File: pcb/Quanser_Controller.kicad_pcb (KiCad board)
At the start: 2 copper layers, 115.6 x 61 mm, 19 parts, among them J1 Conn_02x08, J2 Connector Encoder, J3 Conn_01x10, J4 Conn_01x08, J5 Conn_01x08, J6 Conn_Coaxial, J7 Screw_Terminal_01x02, U1 LMD18200, U2 LS7366R, U3 74LVC1G04

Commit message: Update project.
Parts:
- added F1: 5A, Fuse:Fuseholder_Cylinder-5x20mm_Schurter_0031_8201_Horizontal_Open, F.Cu at (203.6, 102.3)
- added J6: Screw_Terminal_01x02, TerminalBlock:TerminalBlock_Altech_AK300-2_P5.00mm, F.Cu at (157.7, 145.6)
- added Q1: BC548, Package_TO_SOT_THT:TO-92_Inline, F.Cu at (114.0, 140.6)
- added R4: 5K, Resistor_THT:R_Axial_DIN0204_L3.6mm_D1.6mm_P5.08mm_Horizontal, F.Cu at (176.0, 142.5)
- added R5: 2K, Resistor_THT:R_Axial_DIN0204_L3.6mm_D1.6mm_P5.08mm_Horizontal, F.Cu at (176.0, 145.6)
- F1: value Fuse -> 5A
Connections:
- J1 pad 1: Net-(J1-Pad1) -> GND
- J1 pad 11: Net-(J1-Pad11) -> GND
- J1 pad 13: Net-(J1-Pad13) -> GND
- J1 pad 15: Net-(J1-Pad15) -> GND
- J1 pad 3: Net-(J1-Pad3) -> GND
- J1 pad 5: Net-(J1-Pad5) -> GND
- J1 pad 7: Net-(J1-Pad7) -> GND
- J1 pad 9: Net-(J1-Pad9) -> GND
- J4 pad 4: ENABLE -> DISABLE
- J4 pad 8: Net-(J4-Pad8) -> BRAKE
- U1 pad 4: Net-(U1-Pad4) -> BRAKE
- U1 pad 6: Net-(F1-Pad2) -> Net-(F1-Pad1)

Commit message: update pcb
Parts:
- removed the F1 at (203.6, 102.3)
- removed the F1 at (125.8, 129.7)
- removed the J6 at (157.7, 145.6)
- removed the J6 at (83.1, 107.7)
- removed U3: 74LVC1G04, Connector_PinHeader_2.00mm:PinHeader_2x03_P2.00mm_Vertical
- added F1: 5A, Fuse:Fuseholder_Cylinder-5x20mm_Schurter_0031_8201_Horizontal_Open, F.Cu at (154.9, 76.2)
- added J6: Screw_Terminal_01x02, TerminalBlock:TerminalBlock_Altech_AK300-2_P5.00mm, F.Cu at (97.8, 61.0)
- J7: footprint Connector_PinHeader_2.00mm:PinHeader_1x02_P2.00mm_Vertical -> TerminalBlock:TerminalBlock_Altech_AK300-2_P5.00mm
- moved R5 98.3 mm to (135.9, 55.9)
- moved J7 84.3 mm to (120.7, 61.0)
- moved J2 79.6 mm to (198.1, 59.7)
- moved R4 69.2 mm to (132.1, 88.9), turned to 270 degrees
- moved R2 66.0 mm to (118.1, 88.9), turned to 0 degrees
- moved Q1 64.2 mm to (138.4, 81.3), turned to 90 degrees
- moved J5 58.7 mm to (182.9, 53.3), turned to 90 degrees
- moved J1 56.1 mm to (97.8, 97.8)
- moved J4 53.7 mm to (97.8, 88.9), turned to 90 degrees
- moved C3 52.8 mm to (97.8, 73.7)
- moved C4 49.7 mm to (142.2, 68.6), turned to 90 degrees
- moved U1 46.0 mm to (108.0, 80.0)
- moved U2 43.1 mm to (176.5, 73.7), turned to 90 degrees
- moved R3 39.0 mm to (97.8, 85.1), turned to 90 degrees
- moved C2 34.8 mm to (170.2, 88.9)
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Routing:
- net GND: track 139.3 -> 0.62 mm
- net Net-(R2-Pad2): track 69.0 -> 15.4 mm
- net Net-(F1-Pad1): track 0.00 -> 42.2 mm
- net DISABLE: track 0.00 -> 30.4 mm
- net +5V: track 104.6 -> 125.0 mm
- net Net-(C1-Pad1): track 29.7 -> 47.6 mm
- net Net-(F1-Pad2): track 25.8 -> 43.0 mm
- net TH_FLAG: track 44.2 -> 29.0 mm
- net Net-(U1-Pad4): track 14.7 -> 0.00 mm
- net BRAKE: track 0.00 -> 14.5 mm
- net Net-(C4-Pad2): track 34.6 -> 48.9 mm
- net PWM: track 22.4 -> 9.54 mm
- net Net-(Q1-Pad2): track 0.00 -> 12.2 mm
- net #SS: track 12.0 -> 24.1 mm
- net ENABLE: track 9.76 -> 0.00 mm
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- added copper zone on B.Cu, net GND
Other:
- board size 115.6 x 61 mm -> 114.3 x 50.8 mm

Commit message: update PCB; included reports; add A/D
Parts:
- added AD1: Conn_01x06, Connector_PinHeader_2.00mm:PinHeader_1x06_P2.00mm_Vertical, F.Cu at (92.7, 80.0)
- added R6: 1K, Resistor_THT:R_Axial_DIN0204_L3.6mm_D1.6mm_P5.08mm_Horizontal, F.Cu at (149.9, 86.4)
- added R7: 1K, Resistor_THT:R_Axial_DIN0204_L3.6mm_D1.6mm_P5.08mm_Horizontal, F.Cu at (135.9, 99.1)
- R4: value 5K -> 4K3
- R5: value 2K -> 5K
- moved R5 41.9 mm to (125.7, 96.5), turned to 180 degrees
- moved F1 22.9 mm to (154.9, 53.3), turned to 270 degrees
- turned C1 to 270 degrees
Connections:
- net Net-(R2-Pad2) renamed AD
- F1 pad 1: Net-(F1-Pad1) -> +28V
- J4 pad 4: DISABLE -> ENABLE
- J4 pad 8: BRAKE -> Net-(J4-Pad8)
- Q1 pad 1: Net-(F1-Pad2) -> Net-(Q1-Pad1)
- R4 pad 2: DISABLE -> ENABLE
- R5 pad 1: +28V -> Net-(Q1-Pad2)
- R5 pad 2: Net-(F1-Pad2) -> GND
- U1 pad 4: BRAKE -> Net-(Q1-Pad1)
- U1 pad 5: +5V -> ENABLE
- U1 pad 6: Net-(F1-Pad1) -> Net-(F1-Pad2)
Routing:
- net ENABLE: track 0.00 -> 96.9 mm
- net Net-(Q1-Pad1): track 0.00 -> 88.7 mm
- net Net-(F1-Pad1): track 42.2 -> 0.00 mm
- net DISABLE: track 30.4 -> 0.00 mm
- net AD: track 15.4 -> 44.5 mm
- net +28V: track 17.3 -> 44.9 mm
- net BRAKE: track 14.5 -> 0.00 mm
- net Net-(Q1-Pad2): track 12.2 -> 23.9 mm
- net GND: track 0.62 -> 9.29 mm
- net +5V: track 125.0 -> 129.8 mm
- net TH_FLAG: track 29.0 -> 31.5 mm
- net Net-(J2-Pad4): track 12.7 -> 11.2 mm
- net Net-(J2-Pad5): track 12.7 -> 11.2 mm
- net Net-(C2-Pad1): track 39.1 -> 40.1 mm
- net Net-(J4-Pad8): track 0.00 -> 1.00 mm
- removed copper zone on B.Cu, net GND
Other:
- net class Default: clearance 0.2 -> 0.1778; trace_width 0.25 -> 0.2
- rule trace_clearance: 0.2 -> 0.1778

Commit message: Last update PCB
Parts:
- removed AD1: Conn_01x06, Connector_PinHeader_2.00mm:PinHeader_1x06_P2.00mm_Vertical
- added J8: Conn_01x06, Connector_PinHeader_2.00mm:PinHeader_1x06_P2.00mm_Vertical, F.Cu at (92.7, 81.3)
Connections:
- J4 pad 3: TH_FLAG -> PWM
- J4 pad 7: PWM -> TH_FLAG
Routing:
- net PWM: track 9.54 -> 13.4 mm
- net TH_FLAG: track 31.5 -> 30.9 mm
- net AD: track 44.5 -> 44.0 mm
- added copper zone on F.Cu, net GND
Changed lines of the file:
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@@
     (thickness 1.6)
     (drawings 4)
-    (tracks 140)
+    (tracks 144)
     (zones 0)
     (modules 24)
@@
   (net 47 "Net-(Q1-Pad1)")
   (net 48 AD)
-  (net 49 "Net-(AD1-Pad2)")
-  (net 50 "Net-(AD1-Pad3)")
-  (net 51 "Net-(AD1-Pad4)")
-  (net 52 "Net-(AD1-Pad5)")
-  (net 53 "Net-(AD1-Pad1)")
+  (net 49 "Net-(J8-Pad1)")
+  (net 50 "Net-(J8-Pad2)")
+  (net 51 "Net-(J8-Pad3)")
+  (net 52 "Net-(J8-Pad4)")
+  (net 53 "Net-(J8-Pad5)")
   (net_class Default "This is the default net class."
     (clearance 0.1778)
@@
     (add_net MISO)
     (add_net MOSI)
-    (add_net "Net-(AD1-Pad1)")
-    (add_net "Net-(AD1-Pad2)")
-    (add_net "Net-(AD1-Pad3)")
-    (add_net "Net-(AD1-Pad4)")
-    (add_net "Net-(AD1-Pad5)")
     (add_net "Net-(C1-Pad1)")
     (add_net "Net-(C2-Pad1)")
@@
     (add_net "Net-(J5-Pad4)")
     (add_net "Net-(J5-Pad8)")
+    (add_net "Net-(J8-Pad1)")
+    (add_net "Net-(J8-Pad2)")
+    (add_net "Net-(J8-Pad3)")
+    (add_net "Net-(J8-Pad4)")
+    (add_net "Net-(J8-Pad5)")
     (add_net "Net-(Q1-Pad1)")
     (add_net "Net-(Q1-Pad2)")
@@
       (net 32 "Net-(J4-Pad2)"))
     (pad 3 thru_hole oval (at 0 4 90) (size 1.35 1.35) (drill 0.8) (layers *.Cu *.Mask)
-      (net 33 TH_FLAG))
+      (net 34 PWM))
     (pad 4 thru_hole oval (at 0 6 90) (size 1.35 1.35) (drill 0.8) (layers *.Cu *.Mask)
       (net 45 ENABLE))
@@
       (net 12 ELB2))
     (pad 7 thru_hole oval (at 0 12 90) (size 1.35 1.35) (drill 0.8) (layers *.Cu *.Mask)
-      (net 34 PWM))
+      (net 33 TH_FLAG))
     (pad 8 thru_hole oval (at 0 14 90) (size 1.35 1.35) (drill 0.8) (layers *.Cu *.Mask)
       (net 46 "Net-(J4-Pad8)"))
@@
   )
   (module Connector_PinHeader_2.00mm:PinHeader_1x06_P2.00mm_Vertical (layer F.Cu)
-    (at 92.71 80.01 180)
+    (at 92.71 81.28 180)
     (descr "Through hole straight pin header, 1x06, 2.00mm pitch, single row")
     (tags "Through hole pin header THT 1x06 2.00mm single row")
-    (fp_text reference AD1 (at 0 -2.06 180) (layer F.SilkS)
+    (fp_text reference J8 (at 0 -2.06 180) (layer F.SilkS)
       (effects (font (size 1 1) (thickness 0.15)))
     )
@@
     )
     (pad 1 thru_hole rect (at 0 0 180) (size 1.35 1.35) (drill 0.8) (layers *.Cu *.Mask)
-      (net 53 "Net-(AD1-Pad1)"))
+      (net 49 "Net-(J8-Pad1)"))
     (pad 2 thru_hole oval (at 0 2 180) (size 1.35 1.35) (drill 0.8) (layers *.Cu *.Mask)
-      (net 49 "Net-(AD1-Pad2)"))
+      (net 50 "Net-(J8-Pad2)"))
     (pad 3 thru_hole oval (at 0 4 180) (size 1.35 1.35) (drill 0.8) (layers *.Cu *.Mask)
-      (net 50 "Net-(AD1-Pad3)"))
+      (net 51 "Net-(J8-Pad3)"))
     (pad 4 thru_hole oval (at 0 6 180) (size 1.35 1.35) (drill 0.8) (layers *.Cu *.Mask)
-      (net 51 "Net-(AD1-Pad4)"))
+      (net 52 "Net-(J8-Pad4)"))
     (pad 5 thru_hole oval (at 0 8 180) (size 1.35 1.35) (drill 0.8) (layers *.Cu *.Mask)
-      (net 52 "Net-(AD1-Pad5)"))
+      (net 53 "Net-(J8-Pad5)"))
     (pad 6 thru_hole oval (at 0 10 180) (size 1.35 1.35) (drill 0.8) (layers *.Cu *.Mask)
       (net 48 AD))
@@
   (segment (start 184.15 73.66) (end 184.15 72.39) (width 0.25) (layer B.Cu) (net 28))
   (segment (start 184.15 72.39) (end 186.69 69.85) (width 0.25) (layer B.Cu) (net 28))
-  (segment (start 97.79 85.09) (end 101.6 88.9) (width 0.25) (layer F.Cu) (net 33))
-  (segment (start 101.6 88.9) (end 101.79 88.9) (width 0.25) (layer F.Cu) (net 33))
-  (segment (start 121.55 80.01) (end 121.55 84.19) (width 0.25) (layer F.Cu) (net 33))
-  (segment (start 121.55 84.19) (end 119.38 86.36) (width 0.25) (layer F.Cu) (net 33))
-  (segment (start 104.33 86.36) (end 101.79 88.9) (width 0.25) (layer F.Cu) (net 33))
-  (segment (start 119.38 86.36) (end 104.33 86.36) (width 0.25) (layer F.Cu) (net 33))
-  (segment (start 132.08 93.98) (end 108.87 93.98) (width 0.25) (layer F.Cu) (net 45))
-  (segment (start 108.87 93.98) (end 103.79 88.9) (width 0.25) (layer F.Cu) (net 45))
-  (segment (start 111.35 80.01) (end 111.35 81.2353) (width 0.25) (layer B.Cu) (net 34))
-  (segment (start 111.35 81.2353) (end 109.79 82.7953) (width 0.25) (layer B.Cu) (net 34))
-  (segment (start 109.79 82.7953) (end 109.79 88.9) (width 0.25) (layer B.Cu) (net 34))
-  (segment (start 111.79 88.9) (end 111.79 87.8997) (width 0.25) (layer B.Cu) (net 46))
+  (segment (start 109.79 87.945406) (end 112.645406 85.09) (width 0.2) (layer F.Cu) (net 33))
+  (segment (start 120.650001 80.909999) (end 121.55 80.01) (width 0.2) (layer F.Cu) (net 33))
+  (segment (start 119.38 85.09) (end 120.65 83.82) (width 0.2) (layer F.Cu) (net 33))
+  (segment (start 109.79 88.9) (end 109.79 87.945406) (width 0.2) (layer F.Cu) (net 33))
+  (segment (start 120.65 83.82) (end 120.650001 80.909999) (width 0.2) (layer F.Cu) (net 33))
+  (segment (start 112.645406 85.09) (end 119.38 85.09) (width 0.2) (layer F.Cu) (net 33))
+  (segment (start 109.79 87.945406) (end 109.535406 87.945406) (width 0.2) (layer F.Cu) (net 33))
+  (segment (start 106.68 85.09) (end 97.79 85.09) (width 0.2) (layer F.Cu) (net 33))
+  (segment (start 109.535406 87.945406) (end 106.68 85.09) (width 0.2) (layer F.Cu) (net 33))
+  (segment (start 101.6 88.9) (end 101.79 88.9) (width 0.25) (layer F.Cu) (net 34))
+  (segment (start 101.79 88.9) (end 106.87 83.82) (width 0.2) (layer B.Cu) (net 34))
+  (segment (start 107.54 83.82) (end 111.35 80.01) (width 0.2) (layer B.Cu) (net 34))
+  (segment (start 106.87 83.82) (end 107.54 83.82) (width 0.2) (layer B.Cu) (net 34))
   (segment (start 123.19 67.31) (end 120.65 64.77) (width 0.5) (layer F.Cu) (net 40))
   (segment (start 128.27 67.31) (end 123.19 67.31) (width 0.5) (layer F.Cu) (net 40))
@@
   (segment (start 132.08 88.9) (end 129.54 88.9) (width 0.25) (layer B.Cu) (net 41))
   (segment (start 129.54 88.9) (end 125.73 92.71) (width 0.25) (layer B.Cu) (net 41))
-  (segment (start 123.19 88.9) (end 123.19 87.8747) (width 0.25) (layer B.Cu) (net 48))
-  (segment (start 123.19 87.8747) (end 123.19 79.4953) (width 0.25) (layer B.Cu) (net 48))
-  (segment (start 123.19 79.4953) (end 119.85 76.1553) (width 0.25) (layer B.Cu) (net 48))
-  (segment (start 119.85 74.93) (end 119.85 76.1553) (width 0.25) (layer B.Cu) (net 48))
+  (segment (start 132.08 93.98) (end 108.87 93.98) (width 0.25) (layer F.Cu) (net 45))
+  (segment (start 108.87 93.98) (end 103.79 88.9) (width 0.25) (layer F.Cu) (net 45))
   (segment (start 132.08 93.98) (end 133.35 93.98) (width 0.25) (layer B.Cu) (net 45))
   (segment (start 135.89 96.52) (end 135.89 99.06) (width 0.25) (layer B.Cu) (net 45))
@@
   (segment (start 114.75 80.01) (end 114.75 79.56) (width 0.2) (layer F.Cu) (net 45))
   (segment (start 114.75 80.01) (end 114.75 99.88) (width 0.25) (layer B.Cu) (net 45))
+  (segment (start 111.79 88.9) (end 111.79 87.8997) (width 0.25) (layer B.Cu) (net 46))
   (segment (start 138.43 81.28) (end 142.24 81.28) (width 0.25) (layer B.Cu) (net 47))
   (segment (start 142.24 81.28) (end 144.78 83.82) (width 0.25) (layer B.Cu) (net 47))
@@
   (segment (start 138.43 53.34) (end 115.57 53.34) (width 0.25) (layer B.Cu) (net 47))
   (segment (start 113.05 55.86) (end 113.05 74.47999) (width 0.25) (layer B.Cu) (net 47))
-  (segment (start 114.93 70.01) (end 119.85 74.93) (width 0.2) (layer F.Cu) (net 48))
-  (segment (start 92.71 70.01) (end 114.93 70.01) (width 0.2) (layer F.Cu) (net 48))
+  (segment (start 123.19 88.9) (end 123.19 87.8747) (width 0.25) (layer B.Cu) (net 48))
+  (segment (start 123.19 87.8747) (end 123.19 79.4953) (width 0.25) (layer B.Cu) (net 48))
+  (segment (start 123.19 79.4953) (end 119.85 76.1553) (width 0.25) (layer B.Cu) (net 48))
+  (segment (start 119.85 74.93) (end 119.85 76.1553) (width 0.25) (layer B.Cu) (net 48))
+  (segment (start 116.2 71.28) (end 119.85 74.93) (width 0.2) (layer F.Cu) (net 48))
+  (segment (start 92.71 71.28) (end 116.2 71.28) (width 0.2) (layer F.Cu) (net 48))
+  (zone (net 2) (net_name GND) (layer F.Cu) (hatch edge 0.508)
+    (connect_pads (clearance 0.65))
+    (min_thickness 0.254)
+    (fill yes (arc_segments 16) (thermal_gap 0.508) (thermal_bridge_width 0.508))
+    (polygon
+      (pts
+        (xy 88.9 50.8) (xy 203.2 50.8) (xy 203.2 101.6) (xy 88.9 101.6)
+      )
+    )
+  )
 )

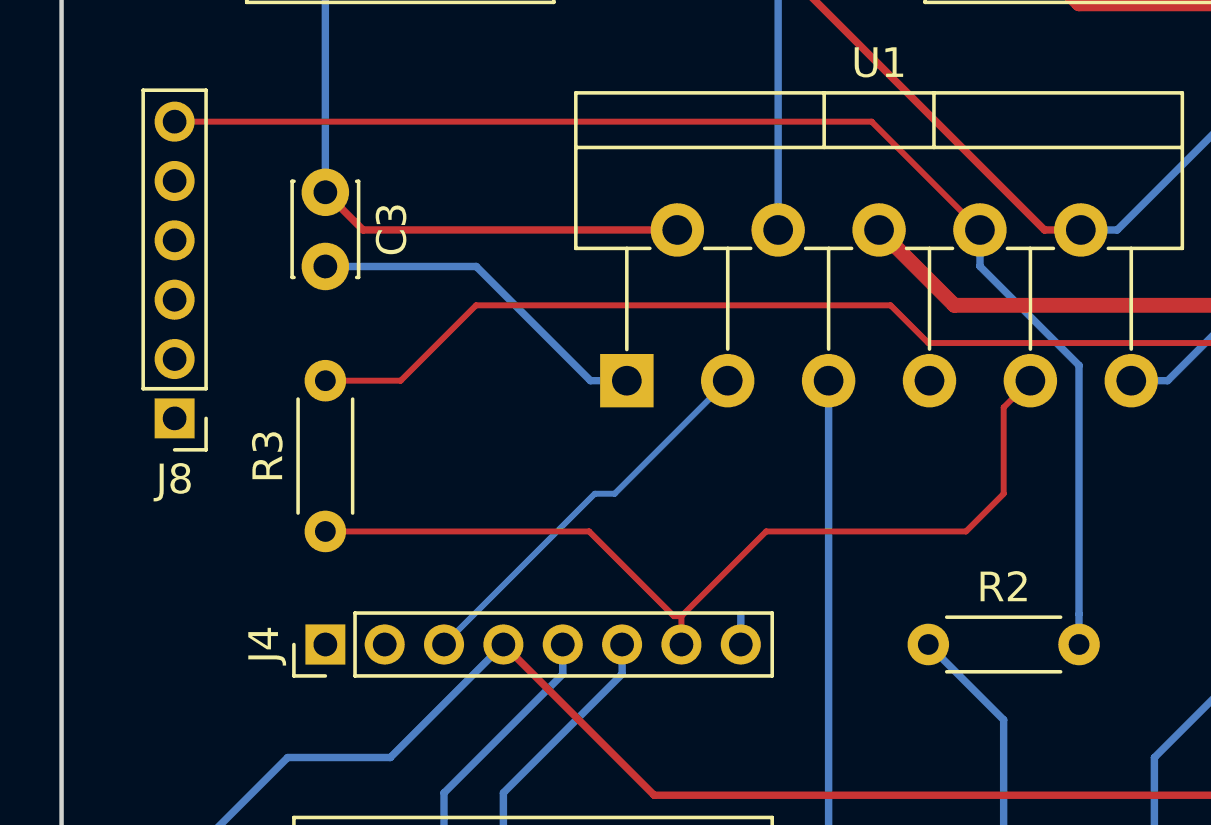
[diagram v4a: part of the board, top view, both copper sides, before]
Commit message: included H-Bridge
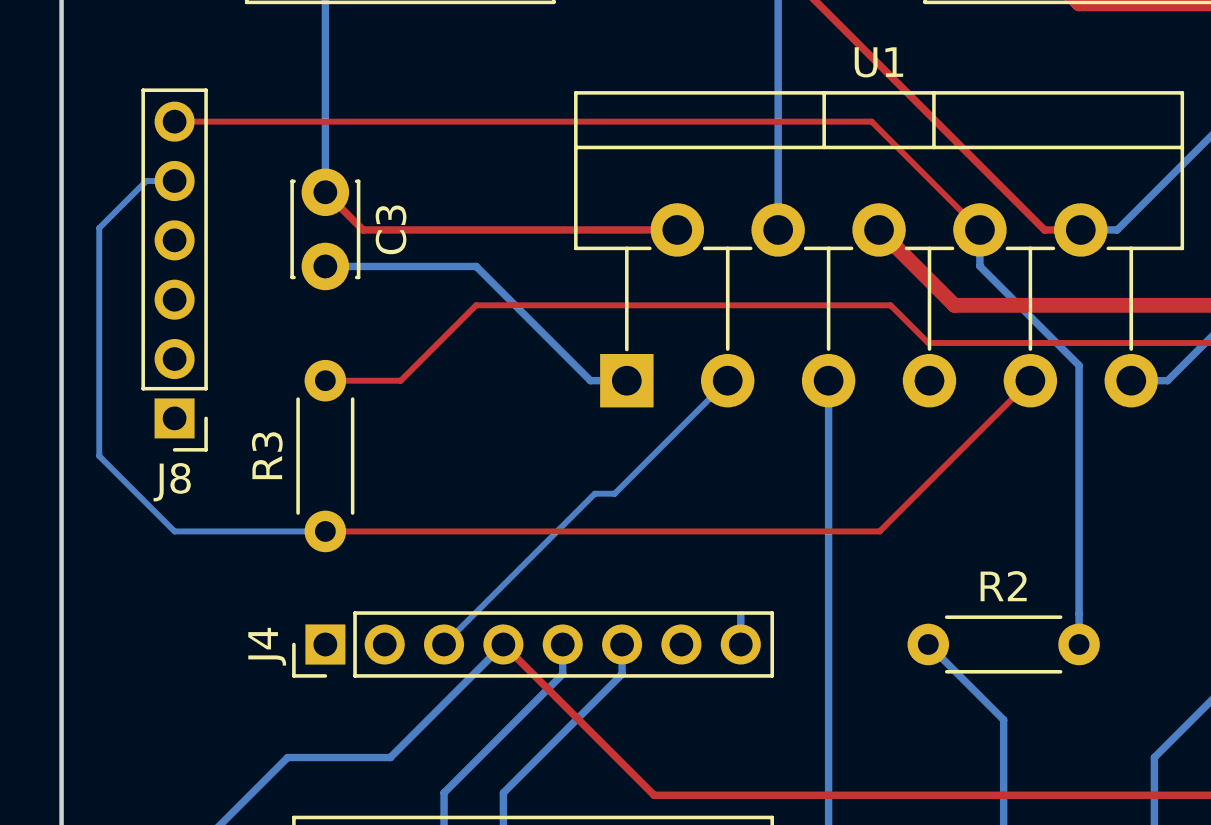
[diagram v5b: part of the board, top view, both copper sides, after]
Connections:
- J4 pad 7: TH_FLAG -> Net-(J4-Pad7)
- J8 pad 5: Net-(J8-Pad5) -> TH_FLAG
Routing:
- net TH_FLAG: track 30.9 -> 45.4 mm
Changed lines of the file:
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@@
     (thickness 1.6)
     (drawings 4)
-    (tracks 144)
+    (tracks 142)
     (zones 0)
     (modules 24)
@@
   (net 51 "Net-(J8-Pad3)")
   (net 52 "Net-(J8-Pad4)")
-  (net 53 "Net-(J8-Pad5)")
+  (net 53 "Net-(J4-Pad7)")
   (net_class Default "This is the default net class."
     (clearance 0.1778)
@@
     (add_net "Net-(J4-Pad1)")
     (add_net "Net-(J4-Pad2)")
+    (add_net "Net-(J4-Pad7)")
     (add_net "Net-(J4-Pad8)")
     (add_net "Net-(J5-Pad1)")
@@
     (add_net "Net-(J8-Pad3)")
     (add_net "Net-(J8-Pad4)")
-    (add_net "Net-(J8-Pad5)")
     (add_net "Net-(Q1-Pad1)")
     (add_net "Net-(Q1-Pad2)")
@@
       (net 12 ELB2))
     (pad 7 thru_hole oval (at 0 12 90) (size 1.35 1.35) (drill 0.8) (layers *.Cu *.Mask)
-      (net 33 TH_FLAG))
+      (net 53 "Net-(J4-Pad7)"))
     (pad 8 thru_hole oval (at 0 14 90) (size 1.35 1.35) (drill 0.8) (layers *.Cu *.Mask)
       (net 46 "Net-(J4-Pad8)"))
@@
       (net 52 "Net-(J8-Pad4)"))
     (pad 5 thru_hole oval (at 0 8 180) (size 1.35 1.35) (drill 0.8) (layers *.Cu *.Mask)
-      (net 53 "Net-(J8-Pad5)"))
+      (net 33 TH_FLAG))
     (pad 6 thru_hole oval (at 0 10 180) (size 1.35 1.35) (drill 0.8) (layers *.Cu *.Mask)
       (net 48 AD))
@@
   (segment (start 184.15 73.66) (end 184.15 72.39) (width 0.25) (layer B.Cu) (net 28))
   (segment (start 184.15 72.39) (end 186.69 69.85) (width 0.25) (layer B.Cu) (net 28))
-  (segment (start 109.79 87.945406) (end 112.645406 85.09) (width 0.2) (layer F.Cu) (net 33))
-  (segment (start 120.650001 80.909999) (end 121.55 80.01) (width 0.2) (layer F.Cu) (net 33))
-  (segment (start 119.38 85.09) (end 120.65 83.82) (width 0.2) (layer F.Cu) (net 33))
-  (segment (start 109.79 88.9) (end 109.79 87.945406) (width 0.2) (layer F.Cu) (net 33))
-  (segment (start 120.65 83.82) (end 120.650001 80.909999) (width 0.2) (layer F.Cu) (net 33))
-  (segment (start 112.645406 85.09) (end 119.38 85.09) (width 0.2) (layer F.Cu) (net 33))
-  (segment (start 109.79 87.945406) (end 109.535406 87.945406) (width 0.2) (layer F.Cu) (net 33))
-  (segment (start 106.68 85.09) (end 97.79 85.09) (width 0.2) (layer F.Cu) (net 33))
-  (segment (start 109.535406 87.945406) (end 106.68 85.09) (width 0.2) (layer F.Cu) (net 33))
+  (segment (start 116.47 85.09) (end 121.55 80.01) (width 0.2) (layer F.Cu) (net 33))
+  (segment (start 97.79 85.09) (end 116.47 85.09) (width 0.2) (layer F.Cu) (net 33))
+  (segment (start 91.755406 73.28) (end 90.17 74.865406) (width 0.2) (layer B.Cu) (net 33))
+  (segment (start 92.71 73.28) (end 91.755406 73.28) (width 0.2) (layer B.Cu) (net 33))
+  (segment (start 90.17 74.865406) (end 90.17 82.55) (width 0.2) (layer B.Cu) (net 33))
+  (segment (start 92.71 85.09) (end 97.79 85.09) (width 0.2) (layer B.Cu) (net 33))
+  (segment (start 90.17 82.55) (end 92.71 85.09) (width 0.2) (layer B.Cu) (net 33))
   (segment (start 101.6 88.9) (end 101.79 88.9) (width 0.25) (layer F.Cu) (net 34))
   (segment (start 101.79 88.9) (end 106.87 83.82) (width 0.2) (layer B.Cu) (net 34))
